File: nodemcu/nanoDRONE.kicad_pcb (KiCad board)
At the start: 2 copper layers, 87.6 x 87.6 mm, 14 parts, among them J1 3.7V, M1 Motor_DC, M2 Motor_DC, M3 Motor_DC, M4 Motor_DC, Q1 BC547, Q2 BC547, Q3 BC547, Q4 BC547, U1 NodeMCU_1.0_(ESP-12E)

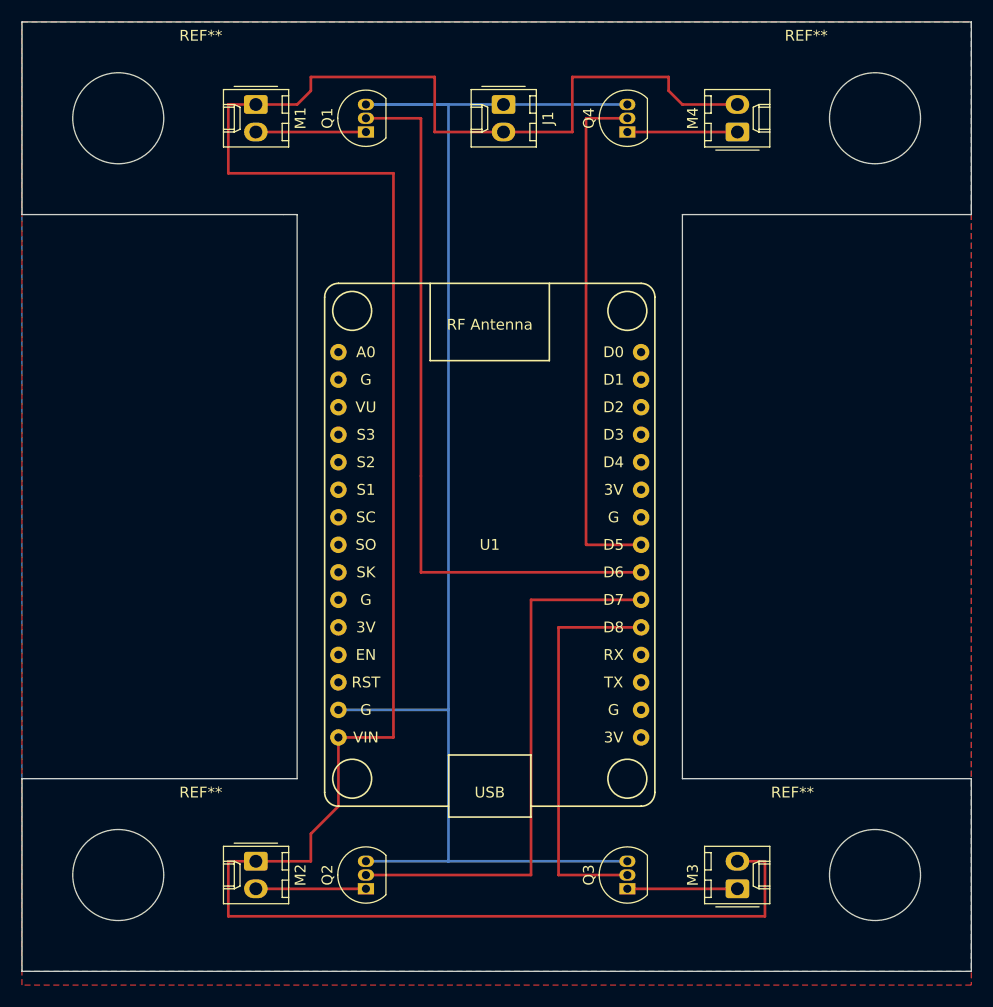
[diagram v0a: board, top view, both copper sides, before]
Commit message: MPU6050 module integrated
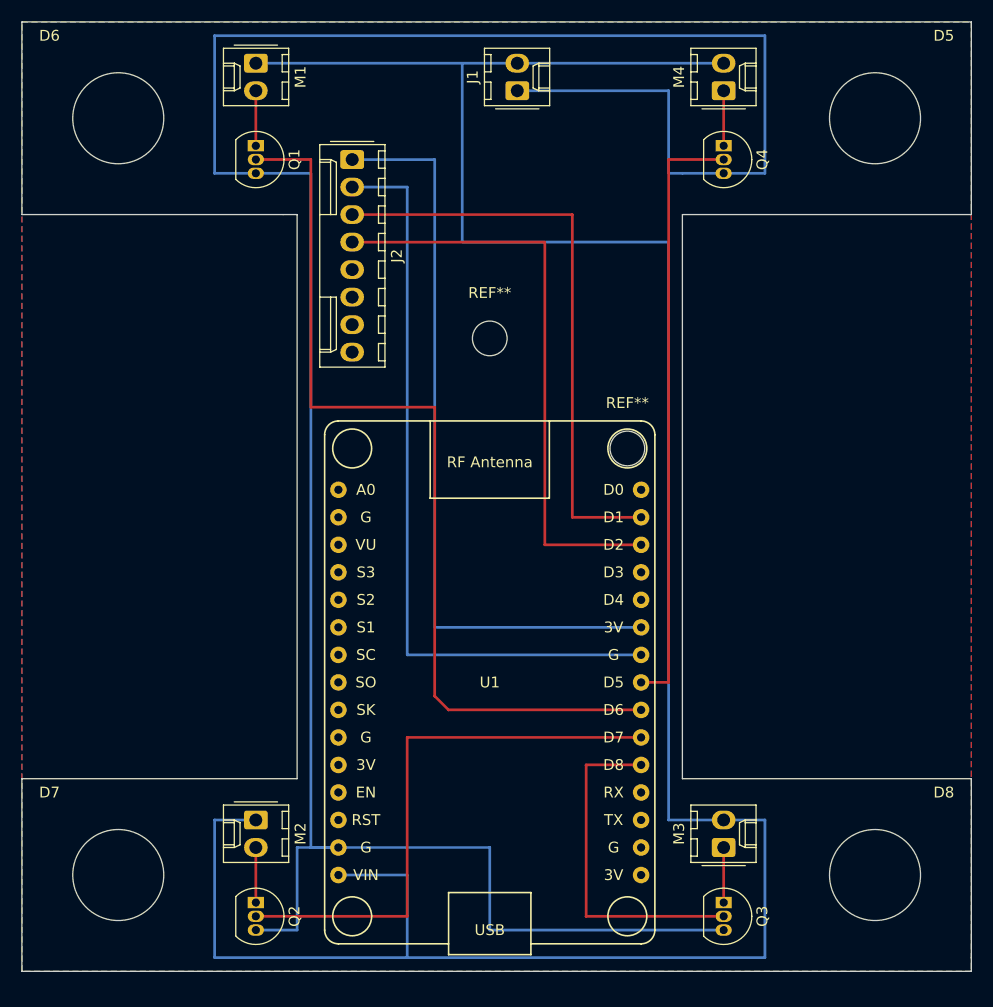
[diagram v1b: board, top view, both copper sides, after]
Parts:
- removed the REF** at (168.9, 85.1)
- removed the REF** at (99.1, 85.1)
- removed the REF** at (99.1, 154.9)
- removed the REF** at (168.9, 154.9)
- added D5: MountingHole_8.4mm_M8, MountingHole:MountingHole_8.4mm_M8, F.Cu at (168.9, 85.1)
- added D6: MountingHole_8.4mm_M8, MountingHole:MountingHole_8.4mm_M8, F.Cu at (99.1, 85.1)
- added D7: MountingHole_8.4mm_M8, MountingHole:MountingHole_8.4mm_M8, F.Cu at (99.1, 154.9)
- added D8: MountingHole_8.4mm_M8, MountingHole:MountingHole_8.4mm_M8, F.Cu at (168.9, 154.9)
- added J2: MPU6050 Dev brd, Connector_Molex:Molex_KK-254_AE-6410-08A_1x08_P2.54mm_Vertical, F.Cu at (120.7, 88.9)
- added REF**: MountingHole_3.2mm_M3, MountingHole:MountingHole_3.2mm_M3, F.Cu at (133.3, 105.4)
- added REF**: MountingHole_3.2mm_M3, MountingHole:MountingHole_3.2mm_M3, F.Cu at (146.1, 115.6)
- moved U1 12.7 mm to (133.3, 137.2)
- moved Q1 10.2 mm to (111.8, 87.6), turned to 270 degrees
- moved Q2 10.2 mm to (111.8, 157.5), turned to 270 degrees
- moved Q4 8.98 mm to (154.9, 87.6), turned to 270 degrees
- moved Q3 8.98 mm to (154.9, 157.5), turned to 270 degrees
- moved M3 4.02 mm to (154.9, 152.4)
- moved M4 4.02 mm to (154.9, 82.5)
- moved M1 3.81 mm to (111.8, 80.0)
- moved M2 3.81 mm to (111.8, 149.9)
- moved J1 1.80 mm to (135.9, 82.5), turned to 90 degrees
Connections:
- U1 pad 24: (no net) -> Net-(J2-Pad2)
- U1 pad 25: (no net) -> Net-(J2-Pad1)
- U1 pad 28: (no net) -> Net-(J2-Pad4)
- U1 pad 29: (no net) -> Net-(J2-Pad3)
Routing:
- net Net-(J1-Pad1): track 135.9 -> 238.8 mm
- net Net-(J2-Pad2): track 0.00 -> 69.8 mm
- net Net-(J2-Pad1): track 0.00 -> 69.8 mm
- net Net-(J2-Pad4): track 0.00 -> 54.6 mm
- net Net-(J2-Pad3): track 0.00 -> 54.6 mm
- net Net-(Q1-Pad2): track 67.3 -> 85.6 mm
- net Net-(J1-Pad2): track 221.8 -> 234.9 mm
- net Net-(Q4-Pad2): track 48.3 -> 55.9 mm
- net Net-(Q3-Pad2): track 36.8 -> 31.7 mm
- net Net-(M3-Pad1): track 10.2 -> 5.08 mm
- net Net-(M2-Pad2): track 10.2 -> 5.08 mm
- net Net-(M4-Pad1): track 10.2 -> 5.08 mm
- net Net-(M1-Pad2): track 10.2 -> 5.08 mm
- net Net-(Q2-Pad2): track 50.8 -> 52.1 mm
- added copper zone on B.Cu, net (none)
- removed copper zone on B.Cu, net Net-(J1-Pad2)

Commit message: names in the silk layer updated
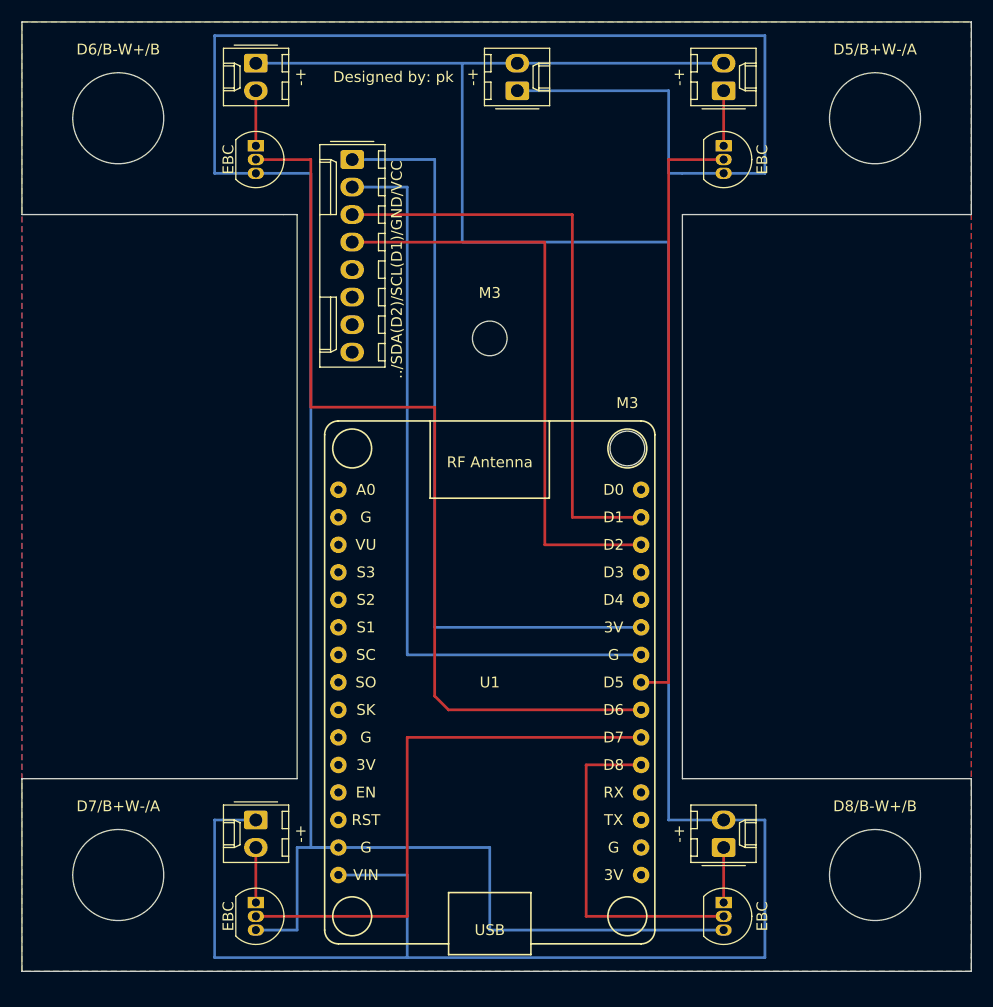
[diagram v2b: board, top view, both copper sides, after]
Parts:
- removed J2: MPU6050 Dev brd, Connector_Molex:Molex_KK-254_AE-6410-08A_1x08_P2.54mm_Vertical
- added ../SDA(D2)/SCL(D1)/GND/VCC: MPU6050 Dev brd, Connector_Molex:Molex_KK-254_AE-6410-08A_1x08_P2.54mm_Vertical, F.Cu at (120.7, 88.9)
- renumbered M2 to -+, M3 to -+, J1 to -+, M1 to -+, M4 to -+, D5 to D5/B+W-/A, D6 to D6/B-W+/B, D7 to D7/B+W-/A, D8 to D8/B-W+/B, Q3 to EBC, Q2 to EBC, Q1 to EBC, Q4 to EBC, REF** to M3
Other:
- board text added: "Designed by: pk"

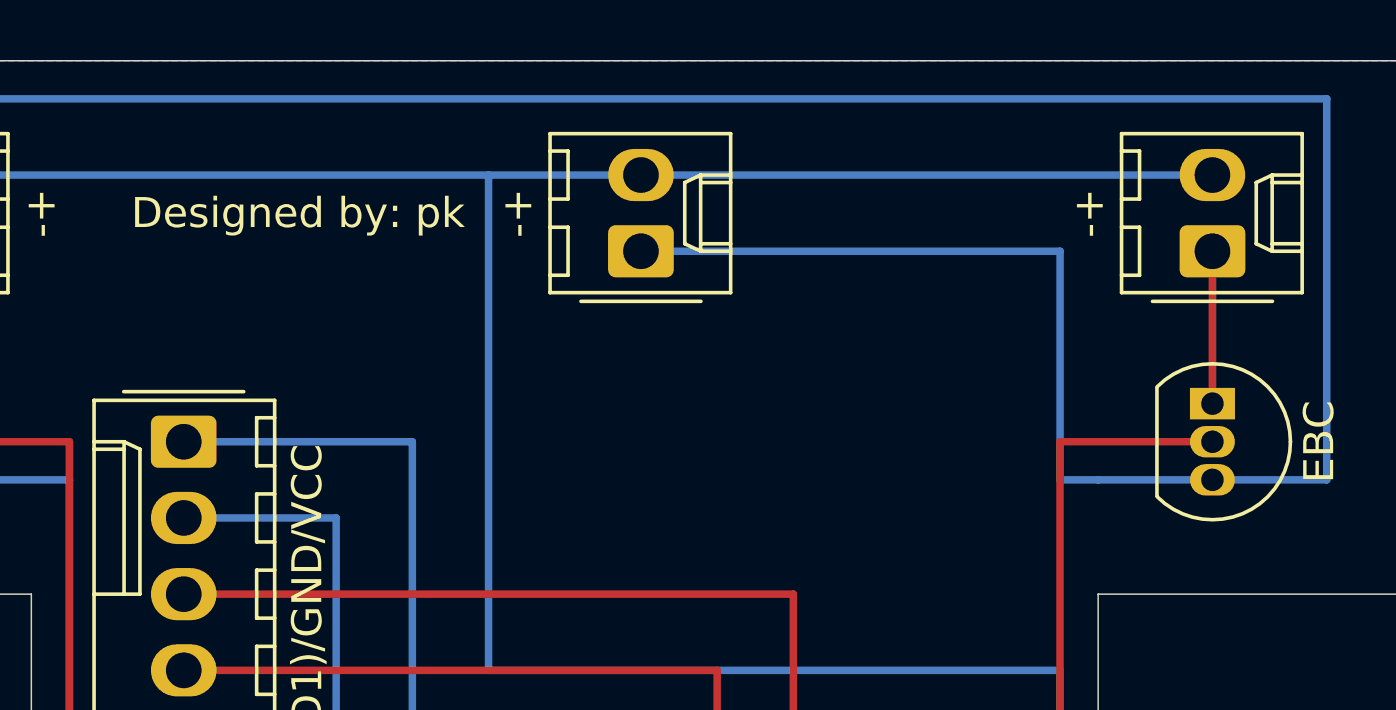
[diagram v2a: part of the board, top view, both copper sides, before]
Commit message: vias added for backside
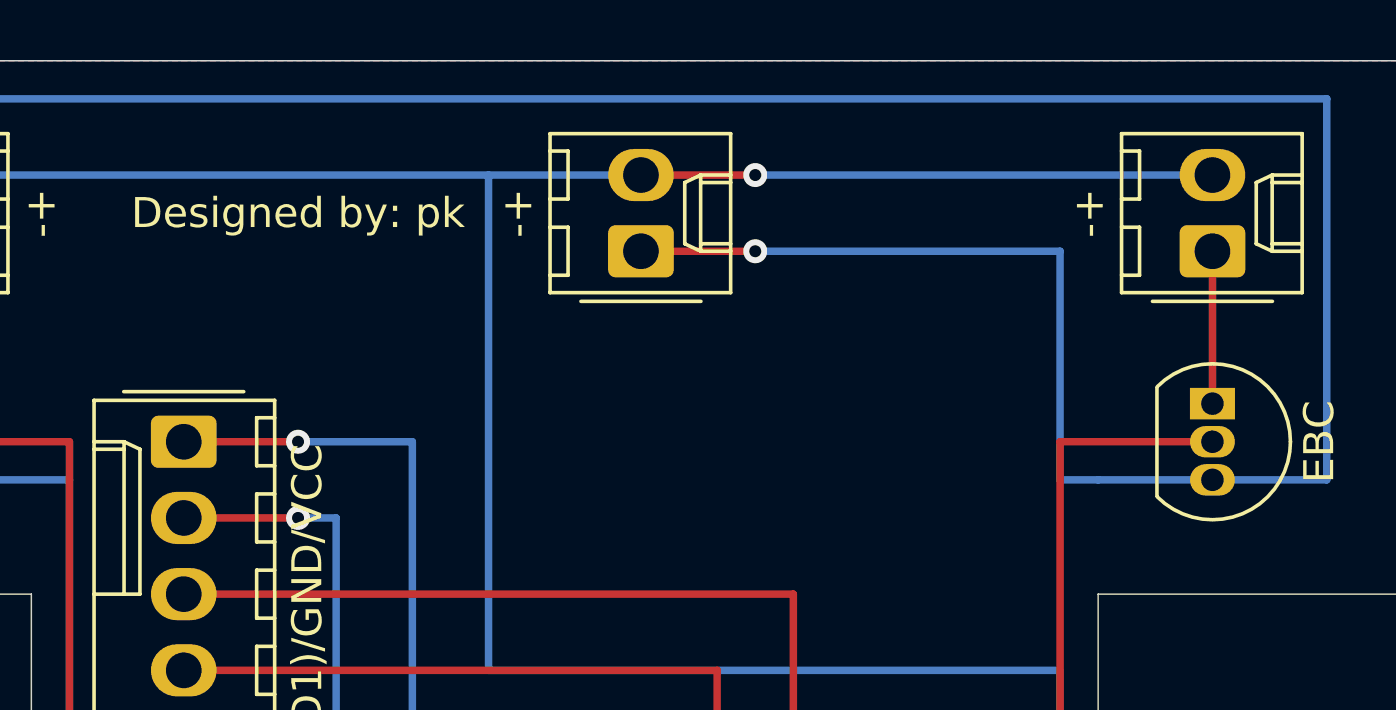
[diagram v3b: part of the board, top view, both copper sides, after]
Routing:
- net Net-(J2-Pad2): vias 0 -> 1
- net Net-(J2-Pad1): vias 0 -> 1
- net Net-(J1-Pad2): vias 0 -> 1
- net Net-(J1-Pad1): vias 0 -> 1
- added copper zone on F.Cu, net (none)
- removed copper zone on F.Cu, net Net-(J1-Pad1)
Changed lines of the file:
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@@
     (thickness 1.6)
     (drawings 20)
-    (tracks 63)
+    (tracks 71)
     (zones 0)
     (modules 17)
@@
     (pad_to_mask_clearance 0.05)
     (aux_axis_origin 0 0)
-    (visible_elements FFFFFF7F)
+    (visible_elements FFFFFFFF)
     (pcbplotparams
       (layerselection 0x010fc_ffffffff)
@@
   (segment (start 133.35 152.4) (end 133.35 160.02) (width 0.25) (layer B.Cu) (net 1))
   (segment (start 133.35 160.02) (end 154.94 160.02) (width 0.25) (layer B.Cu) (net 1) (status 20))
-  (segment (start 135.89 82.55) (end 149.86 82.55) (width 0.25) (layer B.Cu) (net 1) (status 10))
+  (segment (start 139.7 82.55) (end 149.86 82.55) (width 0.25) (layer B.Cu) (net 1) (status 10))
+  (via (at 139.7 82.55) (size 0.8) (drill 0.4) (layers F.Cu B.Cu) (net 1))
+  (segment (start 135.89 82.55) (end 139.7 82.55) (width 0.25) (layer F.Cu) (net 1))
   (segment (start 111.76 149.86) (end 107.95 149.86) (width 0.25) (layer B.Cu) (net 2) (status 10))
   (segment (start 107.95 149.86) (end 107.95 162.56) (width 0.25) (layer B.Cu) (net 2))
@@
   (segment (start 125.73 162.56) (end 158.75 162.56) (width 0.25) (layer B.Cu) (net 2))
   (segment (start 119.38 154.94) (end 125.73 154.94) (width 0.25) (layer B.Cu) (net 2) (status 10))
-  (segment (start 135.89 80.01) (end 154.94 80.01) (width 0.25) (layer B.Cu) (net 2) (status 30))
   (segment (start 135.89 80.01) (end 111.76 80.01) (width 0.25) (layer B.Cu) (net 2) (status 30))
   (segment (start 154.94 149.86) (end 149.86 149.86) (width 0.25) (layer B.Cu) (net 2) (status 10))
@@
   (segment (start 130.81 96.52) (end 130.81 80.01) (width 0.25) (layer B.Cu) (net 2))
   (segment (start 125.73 154.94) (end 125.73 162.56) (width 0.25) (layer B.Cu) (net 2))
+  (segment (start 139.7 80.01) (end 154.94 80.01) (width 0.25) (layer B.Cu) (net 2) (status 30))
+  (via (at 139.7 80.01) (size 0.8) (drill 0.4) (layers F.Cu B.Cu) (net 2))
+  (segment (start 139.7 80.01) (end 135.89 80.01) (width 0.25) (layer F.Cu) (net 2))
   (segment (start 111.76 82.55) (end 111.76 87.63) (width 0.25) (layer F.Cu) (net 3) (status 30))
   (segment (start 154.94 82.55) (end 154.94 87.63) (width 0.25) (layer F.Cu) (net 4) (status 30))
@@
   (segment (start 111.76 152.4) (end 111.76 157.48) (width 0.25) (layer F.Cu) (net 9) (status 30))
   (segment (start 154.94 157.48) (end 154.94 152.4) (width 0.25) (layer F.Cu) (net 10) (status 30))
-  (segment (start 120.65 88.9) (end 128.27 88.9) (width 0.25) (layer B.Cu) (net 11) (status 10))
   (segment (start 128.27 88.9) (end 128.27 132.08) (width 0.25) (layer B.Cu) (net 11))
   (segment (start 128.27 132.08) (end 147.32 132.08) (width 0.25) (layer B.Cu) (net 11) (status 20))
-  (segment (start 120.65 91.44) (end 125.73 91.44) (width 0.25) (layer B.Cu) (net 12) (status 10))
+  (segment (start 124.46 88.9) (end 128.27 88.9) (width 0.25) (layer B.Cu) (net 11) (status 10))
+  (via (at 124.46 88.9) (size 0.8) (drill 0.4) (layers F.Cu B.Cu) (net 11))
+  (segment (start 124.46 88.9) (end 120.65 88.9) (width 0.25) (layer F.Cu) (net 11))
   (segment (start 125.73 91.44) (end 125.73 134.62) (width 0.25) (layer B.Cu) (net 12))
   (segment (start 125.73 134.62) (end 147.32 134.62) (width 0.25) (layer B.Cu) (net 12) (status 20))
+  (segment (start 124.46 91.44) (end 125.73 91.44) (width 0.25) (layer B.Cu) (net 12) (status 10))
+  (via (at 124.46 91.44) (size 0.8) (drill 0.4) (layers F.Cu B.Cu) (net 12))
+  (segment (start 124.46 91.44) (end 120.65 91.44) (width 0.25) (layer F.Cu) (net 12))
   (segment (start 140.97 121.92) (end 147.32 121.92) (width 0.25) (layer F.Cu) (net 13))
   (segment (start 140.97 93.98) (end 140.97 121.92) (width 0.25) (layer F.Cu) (net 13))
@@
   (segment (start 138.43 96.52) (end 138.43 124.46) (width 0.25) (layer F.Cu) (net 14))
   (segment (start 138.43 124.46) (end 147.32 124.46) (width 0.25) (layer F.Cu) (net 14))
-  (zone (net 1) (net_name "Net-(J1-Pad1)") (layer F.Cu) (hatch edge 0.508)
+  (zone (net 0) (net_name "") (layer B.Cu) (hatch edge 0.508)
     (connect_pads (clearance 0.508))
     (min_thickness 0.254)
@@
     )
   )
-  (zone (net 0) (net_name "") (layer B.Cu) (hatch edge 0.508)
+  (zone (net 0) (net_name "") (layer F.Cu) (hatch edge 0.508)
     (connect_pads (clearance 0.508))
     (min_thickness 0.254)

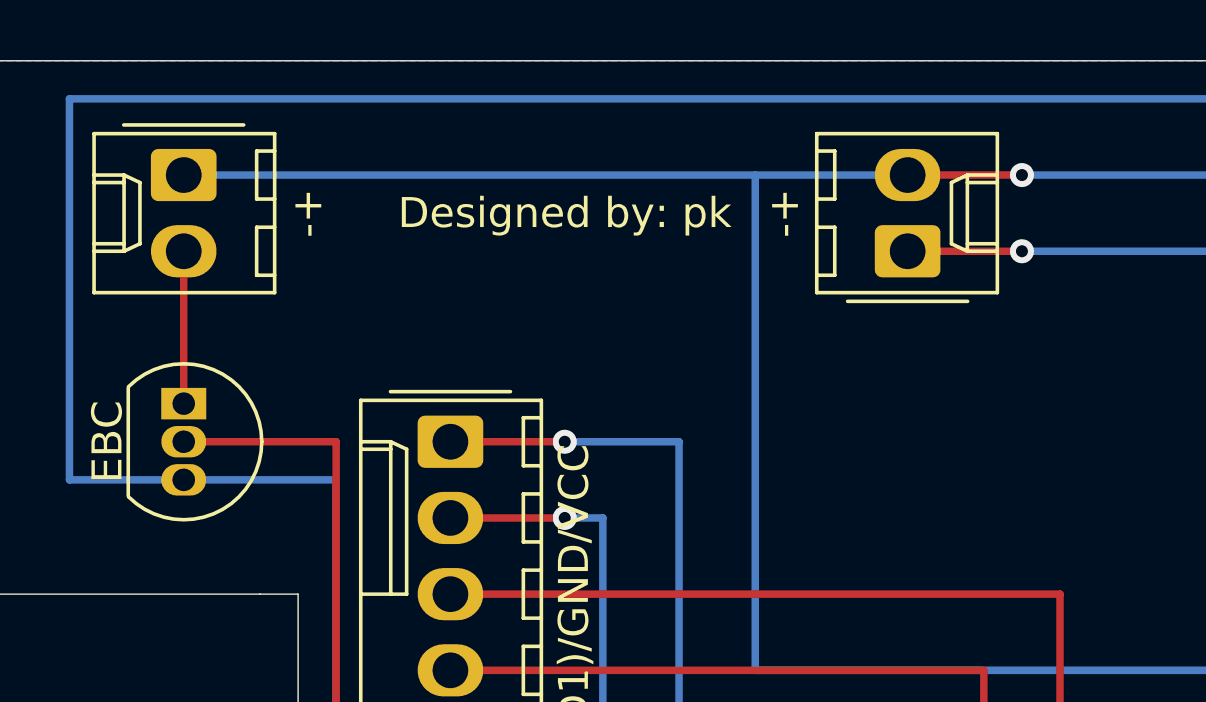
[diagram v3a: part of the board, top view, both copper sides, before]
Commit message: vias review finding fixed
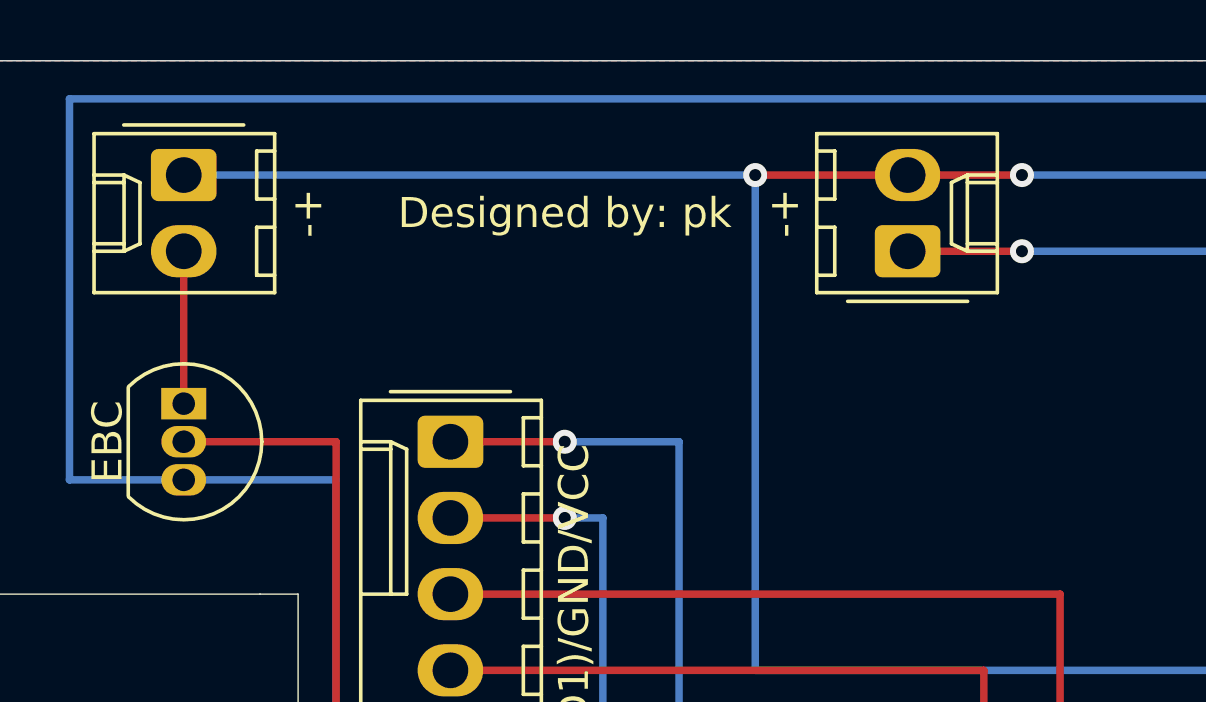
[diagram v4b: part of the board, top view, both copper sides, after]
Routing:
- net Net-(J1-Pad2): vias 1 -> 2
